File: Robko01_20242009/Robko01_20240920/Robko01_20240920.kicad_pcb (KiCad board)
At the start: 2 copper layers, 178.8 x 143.8 mm, 76 parts, among them J1 Conn_01x04_Pin, J10 Motors, J11 Motors, J12 Conn_01x04_Pin, J13 Conn_01x02_Pin, J14 Conn_01x04_Pin, J15 Conn_01x02_Pin, J16 Conn_01x04_Pin, J17 Conn_01x02_Male, J18 Conn_01x02_Male, J19 Conn_01x02_Male, J2 Conn_01x02_Pin, J20 Conn_01x02_Male, J21 Conn_01x19_Pin, J22 Conn_01x19_Pin, J23 Conn_02x05_Odd_Even, J24 USB_A, J25 USB_B, J28 Conn_01x02_Male, J29 Conn_01x07_Pin, J3 Conn_01x02_Pin, J30 Conn_01x02_Male, J31 Conn_02x05_Odd_Even, J4 Conn_01x04_Pin, J5 Conn_01x02_Pin, J6 Conn_01x04_Pin, J7 Conn_01x02_Male, J8 Conn_01x02_Pin, J9 Motors, K2 G5V-2, SW1 SW_DIP_x04, SW2 SW_DIP_x04, SW3 SW_DIP_x04, SW4 SW_DIP_x04, SW5 SW_DIP_x04, SW7 SW_DIP_x04, U1 LM7805_TO220, U2 PC817

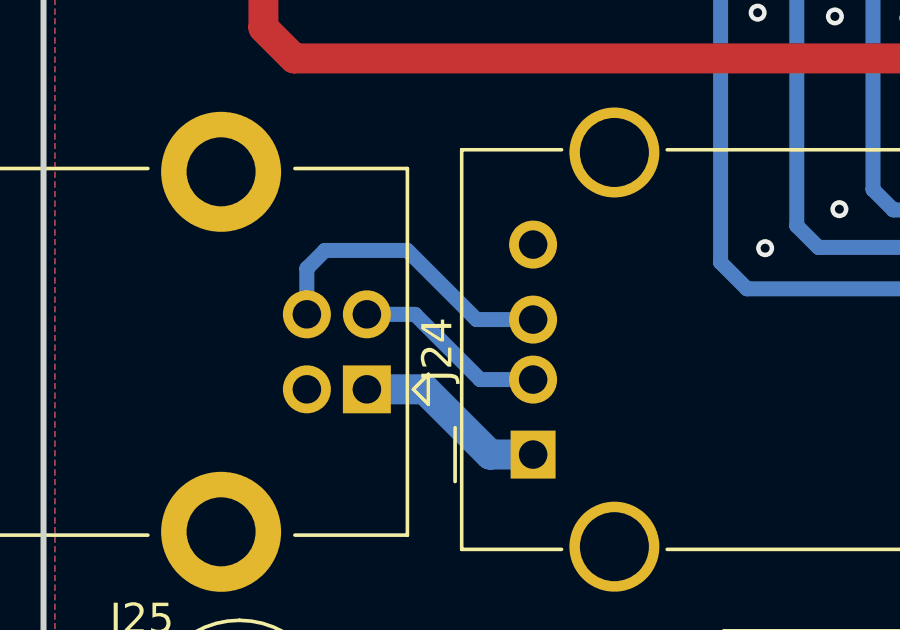
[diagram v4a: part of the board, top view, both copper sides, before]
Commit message: Update USB imp balance
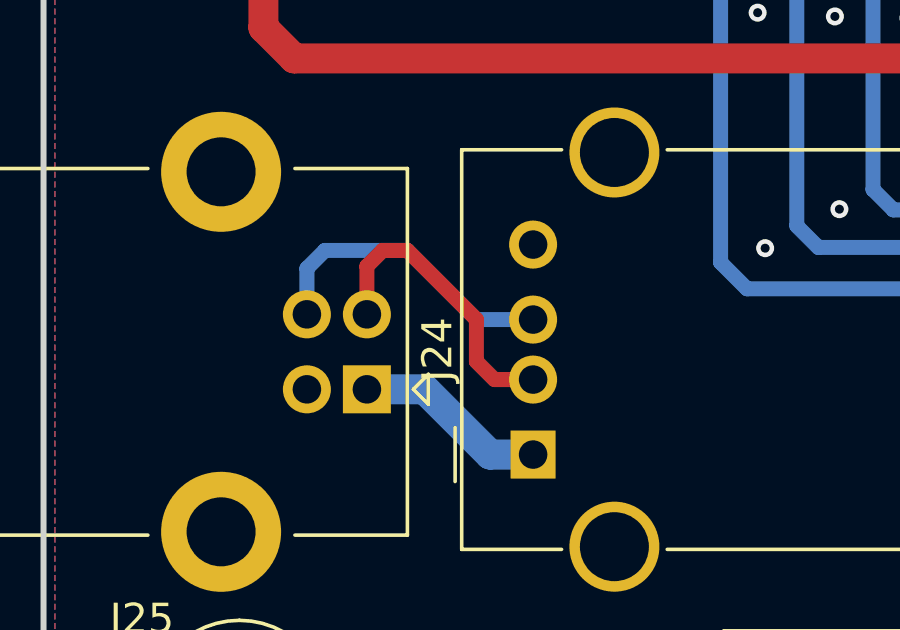
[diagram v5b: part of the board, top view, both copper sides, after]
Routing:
- net Net-(J24-D-): track 6.44 -> 9.97 mm
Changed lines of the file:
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@@
+	)
+	(segment
+		(start 49.95 68.125)
+		(end 49.95 69.73)
+		(width 0.5)
+		(layer "F.Cu")
+		(net 133)
+	)
+	(segment
+		(start 53.6 69.9)
+		(end 51.3 67.6)
+		(width 0.5)
+		(layer "F.Cu")
+		(net 133)
+	)
+	(segment
+		(start 53.6 71.3)
+		(end 53.6 69.9)
+		(width 0.5)
+		(layer "F.Cu")
+		(net 133)
 	)
 	(segment
 		(start 55.49 71.905)
-		(end 53.725 71.905)
+		(end 54.205 71.905)
 		(width 0.5)
-		(layer "B.Cu")
+		(layer "F.Cu")
 		(net 133)
 	)
 	(segment
-		(start 53.725 71.905)
-		(end 51.55 69.73)
+		(start 50.475 67.6)
+		(end 49.95 68.125)
 		(width 0.5)
-		(layer "B.Cu")
+		(layer "F.Cu")
 		(net 133)
 	)
 	(segment
-		(start 49.95 69.73)
-		(end 51.55 69.73)
+		(start 51.3 67.6)
+		(end 50.475 67.6)
 		(width 0.5)
-		(layer "B.Cu")
+		(layer "F.Cu")
 		(net 133)
 	)
+	(segment
+		(start 54.205 71.905)
+		(end 53.6 71.3)
+		(width 0.5)
+		(layer "F.Cu")
+		(net 133)
+	)

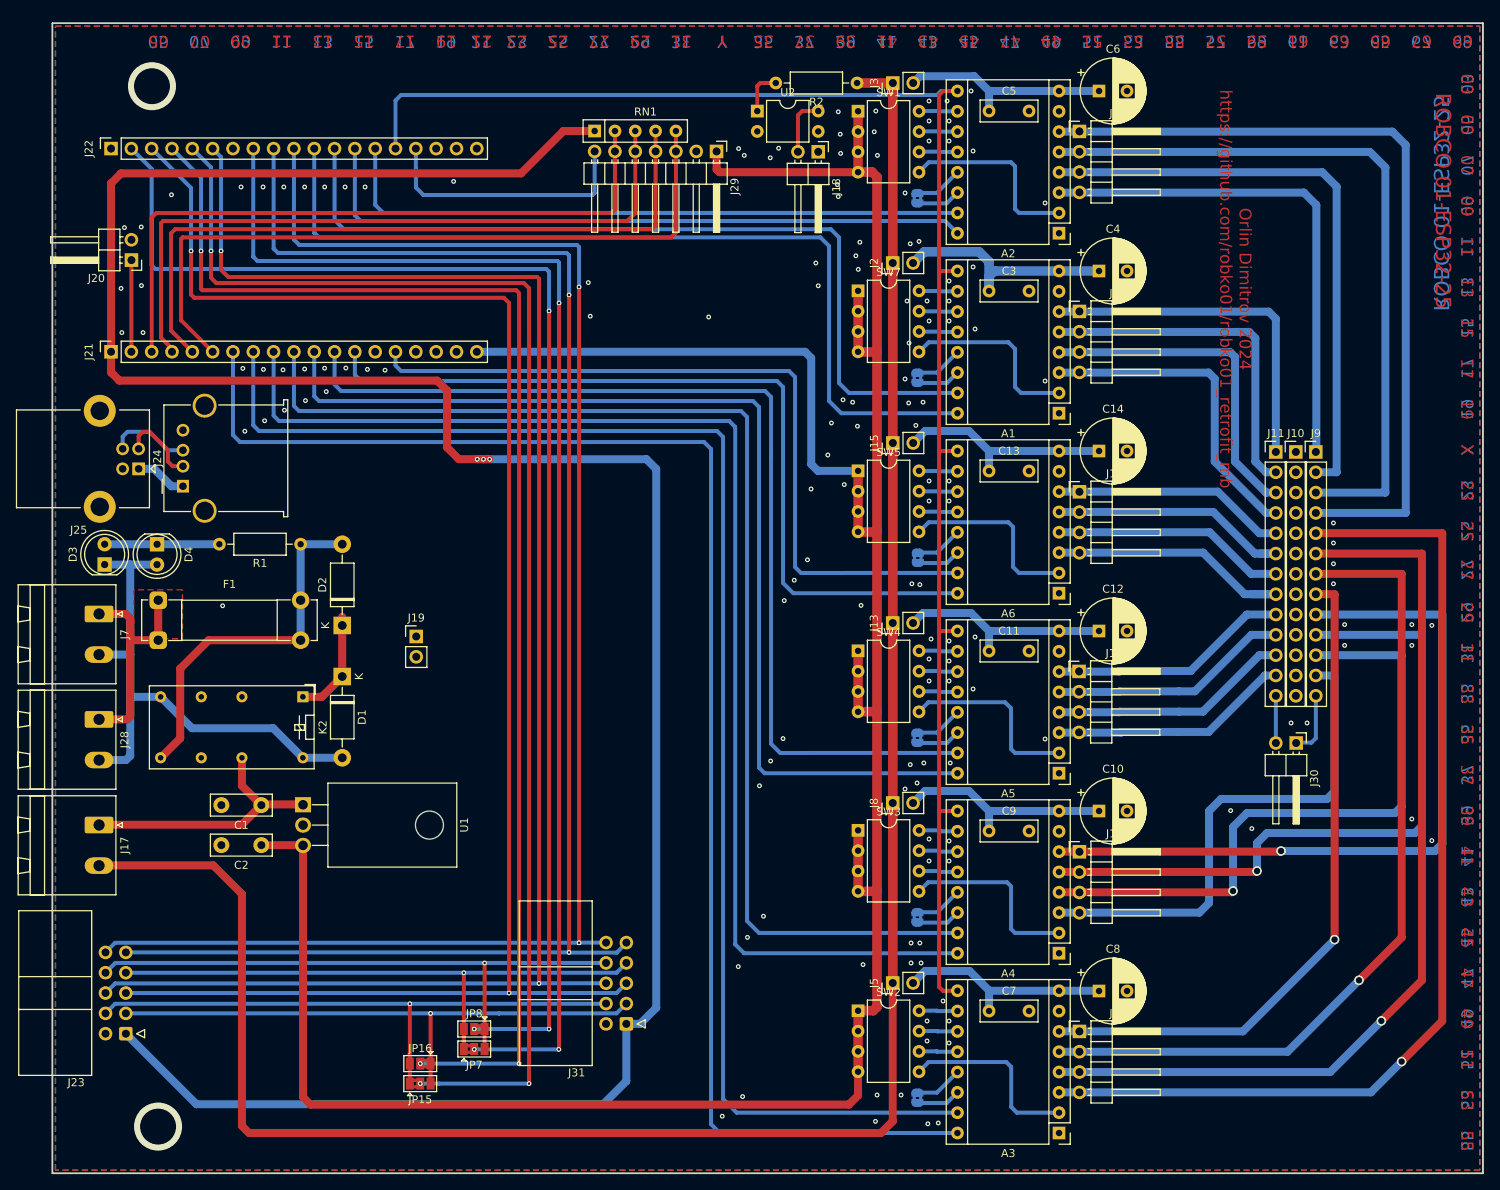
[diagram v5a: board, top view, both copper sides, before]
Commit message: Change E-Stop connector, add default jumper to power supply of the stepper drivers, wireup limit switch of the gripper, rewire E-Stop sensor
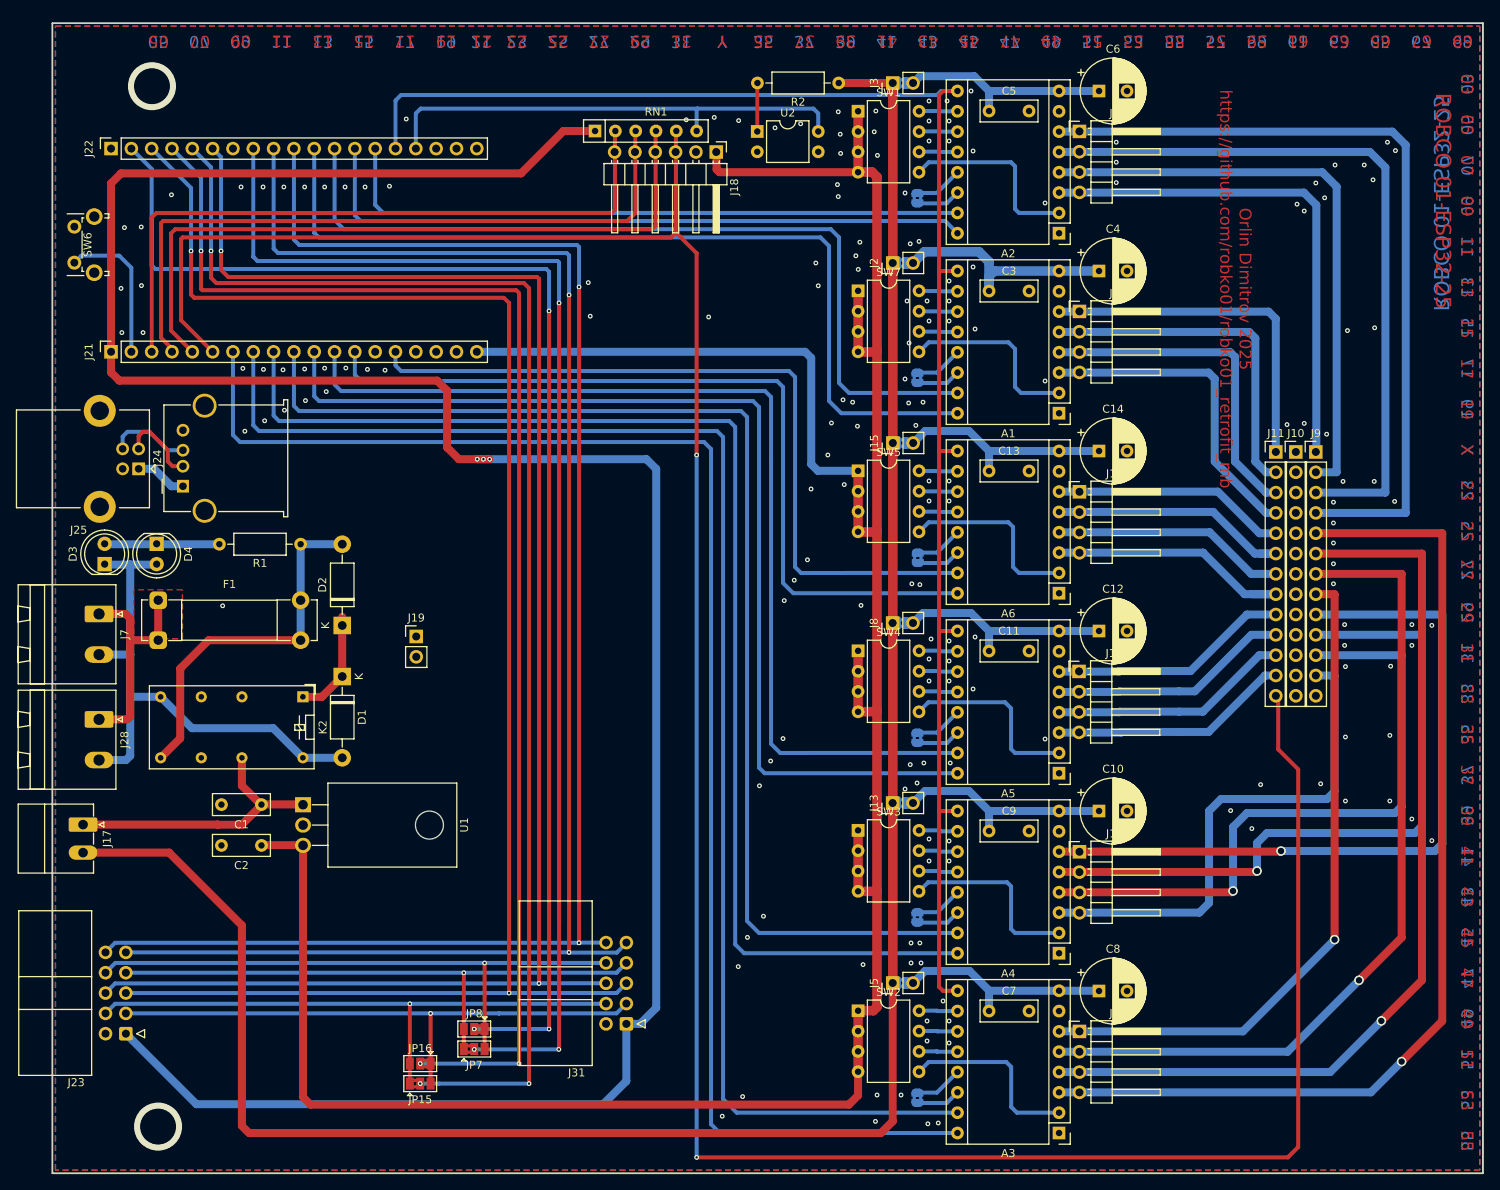
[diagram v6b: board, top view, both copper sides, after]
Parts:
- removed J20, J30: Conn_01x02_Male, Connector_PinHeader_2.54mm:PinHeader_1x02_P2.54mm_Horizontal
- removed J29: Conn_01x07_Pin, Connector_PinHeader_2.54mm:PinHeader_1x07_P2.54mm_Horizontal
- added JP10: SolderJumper_2_Bridged, Jumper:SolderJumper-2_P1.3mm_Bridged2Bar_RoundedPad1.0x1.5mm, B.Cu at (145.3, 24.0)
- added JP11: SolderJumper_2_Bridged, Jumper:SolderJumper-2_P1.3mm_Bridged2Bar_RoundedPad1.0x1.5mm, B.Cu at (145.3, 136.5)
- added JP12: SolderJumper_2_Bridged, Jumper:SolderJumper-2_P1.3mm_Bridged2Bar_RoundedPad1.0x1.5mm, B.Cu at (145.3, 114.0)
- added JP13: SolderJumper_2_Bridged, Jumper:SolderJumper-2_P1.3mm_Bridged2Bar_RoundedPad1.0x1.5mm, B.Cu at (145.3, 91.5)
- added JP14: SolderJumper_2_Bridged, Jumper:SolderJumper-2_P1.3mm_Bridged2Bar_RoundedPad1.0x1.5mm, B.Cu at (145.3, 69.0)
- added JP9: SolderJumper_2_Bridged, Jumper:SolderJumper-2_P1.3mm_Bridged2Bar_RoundedPad1.0x1.5mm, B.Cu at (145.3, 46.5)
- added SW6: RESET, Button_Switch_THT:SW_Tactile_SPST_Angled_PTS645Vx39-2LFS, F.Cu at (41.9, 46.5)
- C1, C2: value 100nF -> 100n; footprint Capacitor_THT:C_Disc_D7.5mm_W2.5mm_P5.00mm -> Capacitor_THT:C_Disc_D7.0mm_W2.5mm_P5.00mm
- D3: value LED -> LED 3mm Green
- D4: value LED -> LED 3mm Red
- J17: footprint Connector_Phoenix_MSTB:PhoenixContact_MSTBA_2,5_2-G-5,08_1x02_P5.08mm_Horizontal -> Connector_Phoenix_MC:PhoenixContact_MC_1,5_2-G-3.5_1x02_P3.50mm_Horizontal
- J18: value Conn_01x02_Male -> Conn_01x06_Pin; footprint Connector_PinHeader_2.54mm:PinHeader_1x02_P2.54mm_Horizontal -> Connector_PinHeader_2.54mm:PinHeader_1x06_P2.54mm_Horizontal
- J19: value Conn_01x02_Male -> TP-GND
- RN1: value R_Network04 -> R_Network05; footprint Resistor_THT:R_Array_SIP5 -> Resistor_THT:R_Array_SIP6
- moved J13 22.5 mm to (144.2, 114.0)
- moved J8 22.5 mm to (144.2, 91.5)
- moved J18 12.8 mm to (122.2, 32.6)
- moved U2 2.55 mm to (127.3, 30.1)
- moved R2 2.29 mm to (137.5, 24.0)
- moved J17 2.00 mm to (43.0, 116.7)
- moved D4 0.08 mm to (52.2, 81.6)
- moved C1 0.07 mm to (65.3, 114.2)
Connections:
- C1 pad 1: MC_POWER -> VCC
- J11 pad 13: GRIPPER_2 -> GPIO35
- J11 pad 3: Net-(A1-1A) -> unconnected-(J11-Pin_3-Pad3)
- J13 pad 2: Net-(A5-VMOT) -> Net-(A4-VMOT)
- J17 pad 1: MC_POWER -> VCC
- J18 pad 1: GND -> +5V
- J18 pad 2: Net-(J18-Pin_2) -> GND
- J21 pad 3: GPIO36 -> M3-Limit
- J21 pad 4: GPIO39 -> M2-Limit
- J21 pad 5: GPIO34 -> M1-Limit
- J21 pad 6: GPIO35 -> M6-Limit
- J22 pad 16: GPIO15 -> E-STOP
- J8 pad 2: Net-(A4-VMOT) -> Net-(A5-VMOT)
- J9 pad 13: GRIPPER_1 -> GND
- K2 pad 13: MC_POWER -> VCC
- RN1 pad 2: GPIO36 -> M3-Limit
- RN1 pad 3: GPIO39 -> M2-Limit
- RN1 pad 4: GPIO34 -> M1-Limit
- RN1 pad 5: GPIO35 -> M6-Limit
- U1 pad 1: MC_POWER -> VCC
- U2 pad 4: Net-(J18-Pin_2) -> E-STOP
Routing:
- net M6-Limit: track 0.00 -> 340.6 mm, vias 0 -> 2
- net GPIO35: track 90.6 -> 0.00 mm
- net M1-Limit: track 0.00 -> 88.7 mm
- net GPIO34: track 88.7 -> 0.00 mm
- net M2-Limit: track 0.00 -> 86.7 mm
- net GPIO39: track 86.7 -> 0.00 mm
- net M3-Limit: track 0.00 -> 84.9 mm
- net GPIO36: track 84.9 -> 0.00 mm
- net E-STOP: track 0.00 -> 60.3 mm
- net VCC: track 0.00 -> 35.5 mm
- net GPIO15: track 32.9 -> 0.00 mm
- net MC_POWER: track 298.5 -> 267.6 mm
- net GRIPPER_1: track 7.99 -> 0.00 mm
- net Net-(J18-Pin_2): track 7.32 -> 0.00 mm
- net MCU_RESET: track 11.5 -> 18.6 mm
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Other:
- board text added: "Orlin Dimitrov 2025 https://github.com/robko01/robko01_retrofit_mb"
- board text removed: "Orlin Dimitrov 2024 https://github.com/robko01/robko01_retrofit_mb"
